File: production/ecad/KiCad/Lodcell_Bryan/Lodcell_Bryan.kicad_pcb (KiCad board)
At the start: 2 copper layers, 22 parts, among them J1 LoadCellConnector, J2 power_for_Loadcell, J3 ConnToESP32, U1 MIC920YC5-TR, U2 MIC920YC5-TR, U3 ADS1231IDR, U4 TXB0104DR

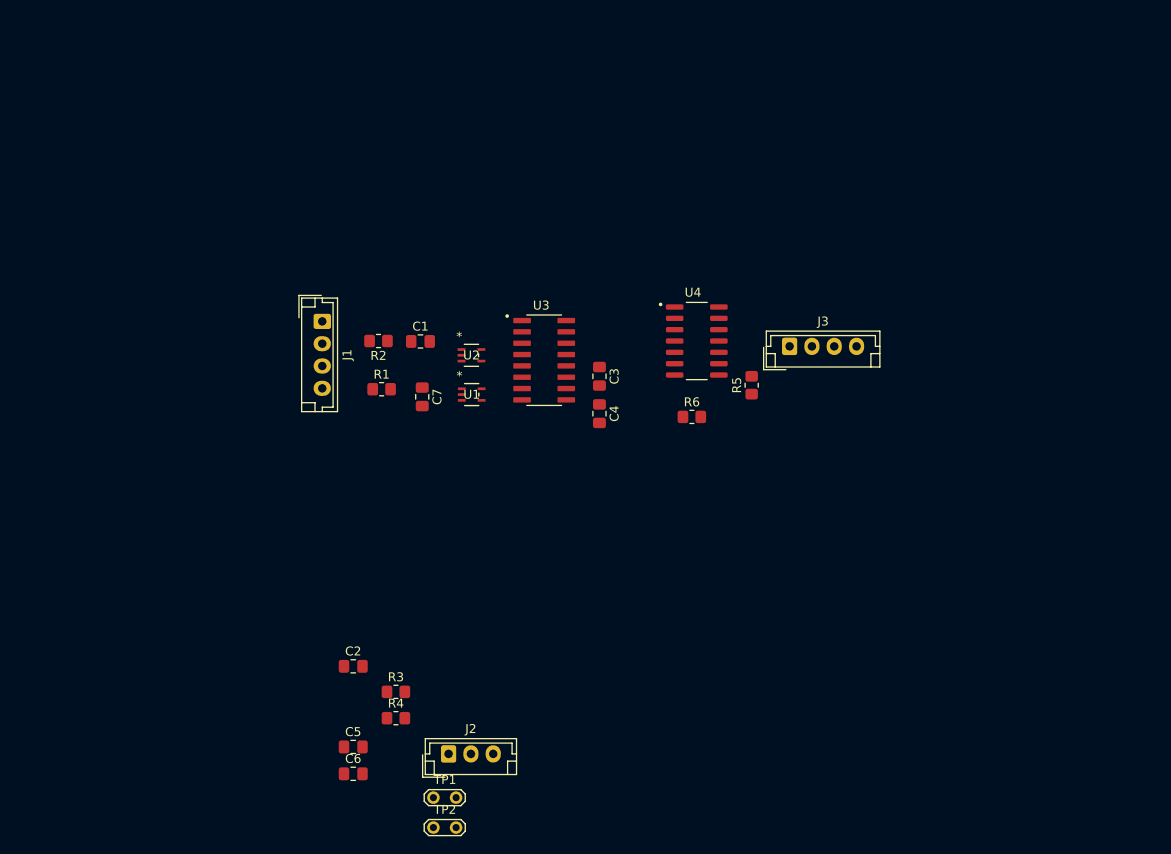
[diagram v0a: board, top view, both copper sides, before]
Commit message: Added mounting holes and very rough layout
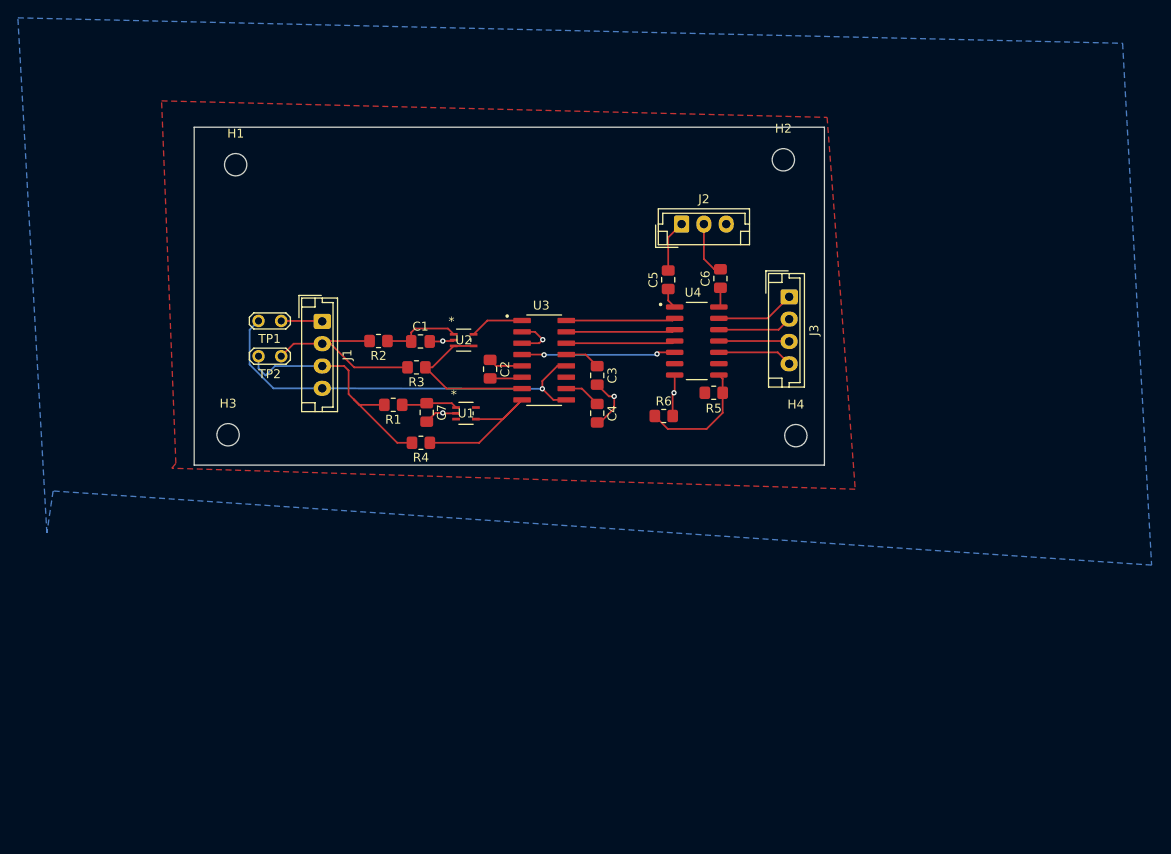
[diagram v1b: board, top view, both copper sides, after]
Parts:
- added H1: MountingHole, MountingHole:MountingHole_2.5mm, F.Cu at (129.8, 45.0)
- added H2: MountingHole, MountingHole:MountingHole_2.5mm, F.Cu at (191.2, 44.5)
- added H3: MountingHole, MountingHole:MountingHole_2.5mm, F.Cu at (129.0, 75.2)
- added H4: MountingHole, MountingHole:MountingHole_2.5mm, F.Cu at (192.6, 75.3)
- moved C6 69.1 mm to (184.2, 57.8), turned to 90 degrees
- moved J2 64.8 mm to (179.8, 51.6)
- moved C5 63.1 mm to (178.3, 57.9), turned to 90 degrees
- moved TP1 56.1 mm to (134.9, 62.5), turned to 180 degrees
- moved TP2 55.5 mm to (134.9, 66.5), turned to 180 degrees
- moved C2 36.7 mm to (158.3, 67.9), turned to -90 degrees
- moved R3 36.4 mm to (150.1, 67.7), turned to 180 degrees
- moved R4 31.0 mm to (150.6, 76.2), turned to 180 degrees
- moved J3 5.55 mm to (191.8, 59.8), turned to -90 degrees
- moved R5 4.33 mm to (183.4, 70.5), turned to 0 degrees
- moved R6 3.15 mm to (177.8, 73.2)
- moved U1 2.19 mm to (155.7, 72.8)
- moved R1 2.18 mm to (147.5, 71.9), turned to 180 degrees
- moved U2 1.91 mm to (155.4, 64.7)
- moved C7 1.82 mm to (151.2, 72.8)
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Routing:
- net Net-(J1-Pin_4): track 0.00 -> 46.7 mm, vias 0 -> 1
- net /RawLoadCell_-: track 0.00 -> 28.1 mm
- net +5V: track 0.00 -> 25.1 mm
- net GND: track 0.00 -> 22.7 mm, vias 0 -> 5
- net /RawLoadCell_+: track 0.00 -> 21.3 mm
- net /LP_-: track 0.00 -> 18.4 mm
- net /LP_+: track 0.00 -> 18.2 mm
- net Net-(U3-SPEED): track 0.00 -> 17.4 mm, vias 0 -> 2
- net Net-(U4-OE): track 0.00 -> 13.4 mm
- net Net-(U3-~{PDWN}): track 0.00 -> 12.2 mm
- net Net-(U3-SCLK): track 0.00 -> 12.2 mm
- net Net-(U3-~{DRDY}/DOUT): track 0.00 -> 12.2 mm
- net Net-(U2-IN+): track 0.00 -> 8.91 mm
- net MISO: track 0.00 -> 8.87 mm
- net Net-(J3-Pin_4): track 0.00 -> 8.41 mm
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- added copper zone on F.Cu, net +5V
- added copper zone on B.Cu, net GND
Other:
- board outline added: 70.6 x 37.9 mm

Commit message: Changes
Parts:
- C5, C6, R5, R6, U4: moved to B.Cu
- moved H3 59.5 mm to (185.0, 55.2)
- moved H1 49.5 mm to (179.3, 45.7)
- moved J3 38.2 mm to (158.5, 78.3), turned to 0 degrees
- moved C6 23.4 mm to (160.8, 60.3)
- moved R5 22.7 mm to (160.7, 70.2), turned to 90 degrees
- moved J2 20.0 mm to (160.7, 57.6)
- moved H4 19.7 mm to (192.2, 55.6)
- moved TP1 18.9 mm to (153.2, 57.4)
- moved TP2 18.8 mm to (152.1, 74.1)
- moved U4 15.9 mm to (165.6, 65.1), turned to 180 degrees
- moved R6 14.6 mm to (163.2, 71.5), turned to -90 degrees
- moved J1 11.1 mm to (150.7, 62.2)
- moved C5 11.0 mm to (167.4, 59.4), turned to 180 degrees
- moved R2 9.82 mm to (155.5, 63.0)
- moved C1 9.19 mm to (159.6, 63.0)
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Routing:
- net Net-(J1-Pin_4): track 46.7 -> 0.00 mm, vias 1 -> 0
- net /RawLoadCell_-: track 28.1 -> 0.00 mm
- net GND: track 22.7 -> 0.00 mm, vias 5 -> 0
- net /RawLoadCell_+: track 21.3 -> 0.00 mm
- net /LP_-: track 18.4 -> 0.00 mm
- net /LP_+: track 18.2 -> 0.00 mm
- net Net-(U3-SPEED): track 17.4 -> 0.00 mm, vias 2 -> 1
- net +5V: track 25.1 -> 7.89 mm
- net Net-(U4-OE): track 13.4 -> 0.00 mm
- net Net-(U3-~{DRDY}/DOUT): track 12.2 -> 2.66 mm
- net Net-(U3-SCLK): track 12.2 -> 2.75 mm
- net Net-(U3-~{PDWN}): track 12.2 -> 2.82 mm
- net Net-(U2-IN+): track 8.91 -> 0.00 mm
- net MISO: track 8.87 -> 0.00 mm
- net Net-(J3-Pin_4): track 8.41 -> 0.00 mm
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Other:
- board size 70.6 x 37.9 mm -> 33.3 x 33.3 mm
- board text added: "+3.3"
- board text added: "+5"
- board text added: "-"
- board text added: "LoadCell"

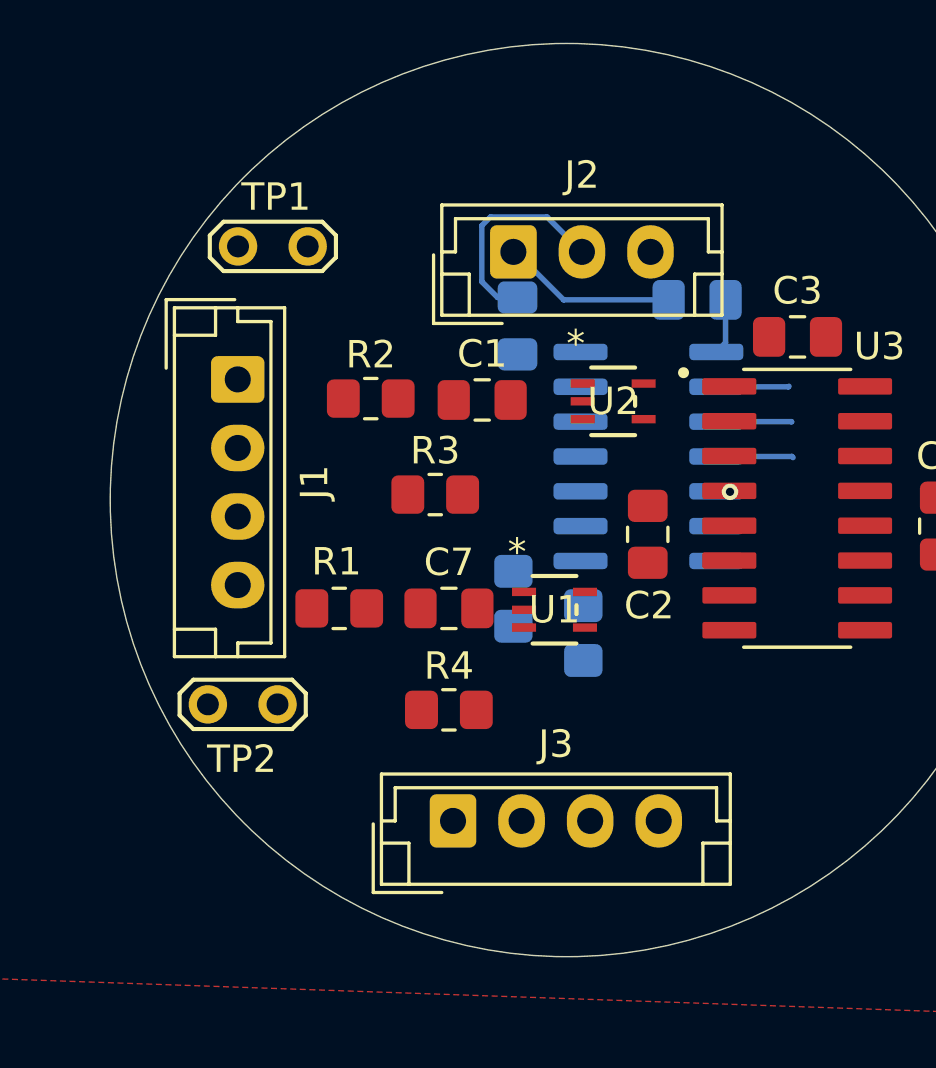
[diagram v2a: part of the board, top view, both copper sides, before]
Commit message: load cell footprint updates
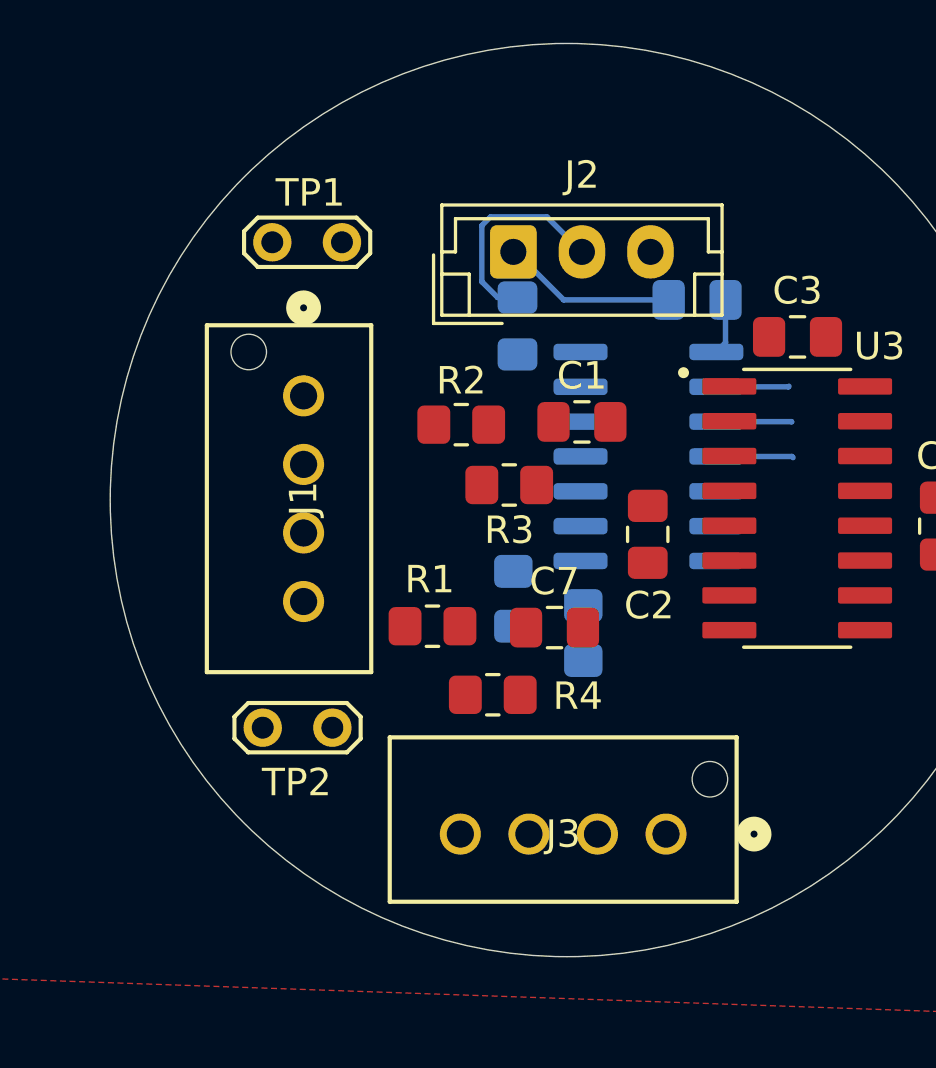
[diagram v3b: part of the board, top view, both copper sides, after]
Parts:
- removed U1, U2: MIC920YC5-TR, MIC920YC5-TR:SC-70_C5_MCH
- H1: value MountingHole -> UpperLeftMH
- H2: value MountingHole -> UpperRightMH
- H3: value MountingHole -> BottomLeftMH
- H4: value MountingHole -> LowerRightMH
- J1, J3: footprint Connector_JST:JST_EH_B4B-EH-A_1x04_P2.50mm_Vertical -> CONN_B4B-XH-AM_JST:CONN_B4B-XH-AM_JST
- moved J3 7.78 mm to (166.3, 78.8)
- moved C7 3.91 mm to (162.2, 71.3)
- moved C1 3.72 mm to (163.2, 63.8)
- moved R1 3.46 mm to (157.8, 71.2)
- moved R2 3.43 mm to (158.8, 63.9)
- moved R3 2.72 mm to (160.6, 66.1)
- moved J1 2.47 mm to (153.1, 62.9), turned to 90 degrees
- moved TP2 2.17 mm to (154.1, 75.0)
- moved R4 1.69 mm to (159.9, 73.8)
- moved TP1 1.26 mm to (154.4, 57.2)
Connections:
- net Net-(J3-Pin_4) renamed SPEED
- C1 pad 1: Net-(U2-IN+) -> /LP_+
- C7 pad 1: Net-(U1-IN+) -> GND
- C7 pad 2: GND -> /LP_-
- R1 pad 1: Net-(U1-IN+) -> /LP_-
- R2 pad 1: Net-(U2-IN+) -> /LP_+
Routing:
- net Net-(U3-SPEED): vias 1 -> 0

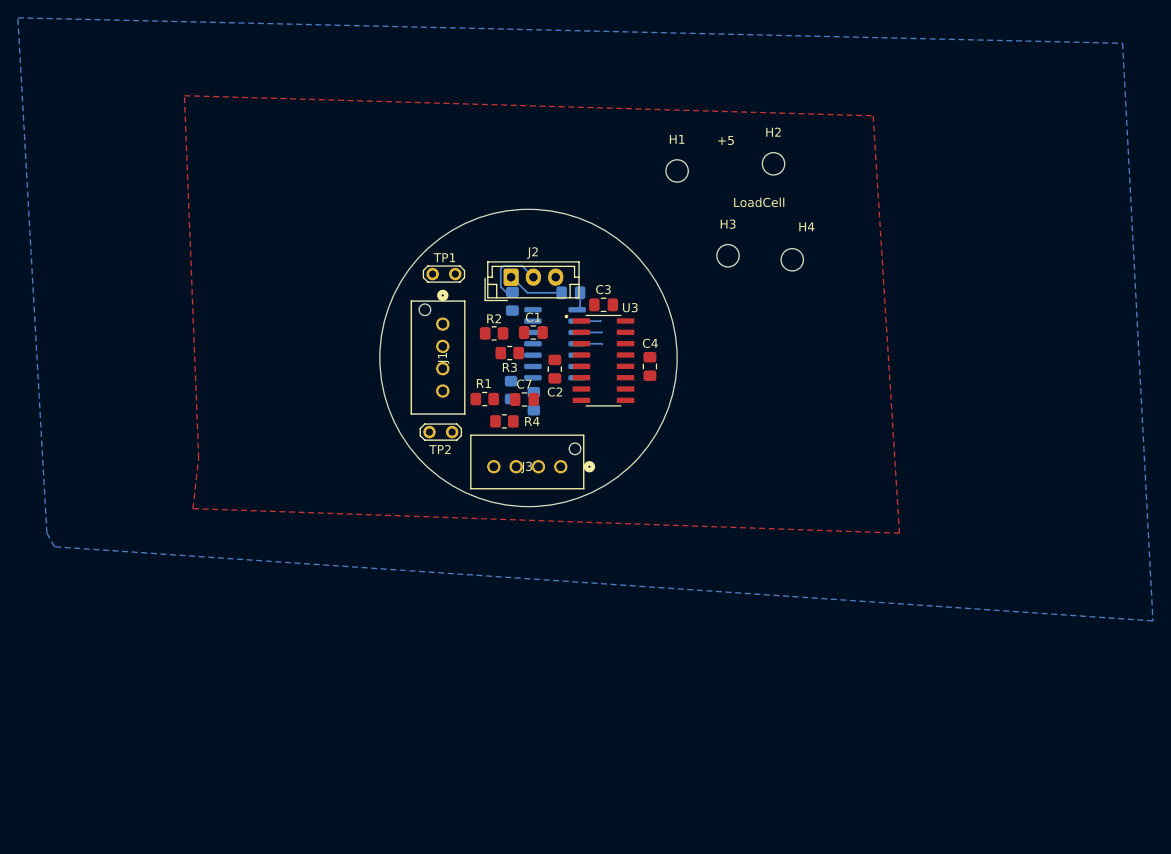
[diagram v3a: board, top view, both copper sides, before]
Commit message: Layout for loadcell
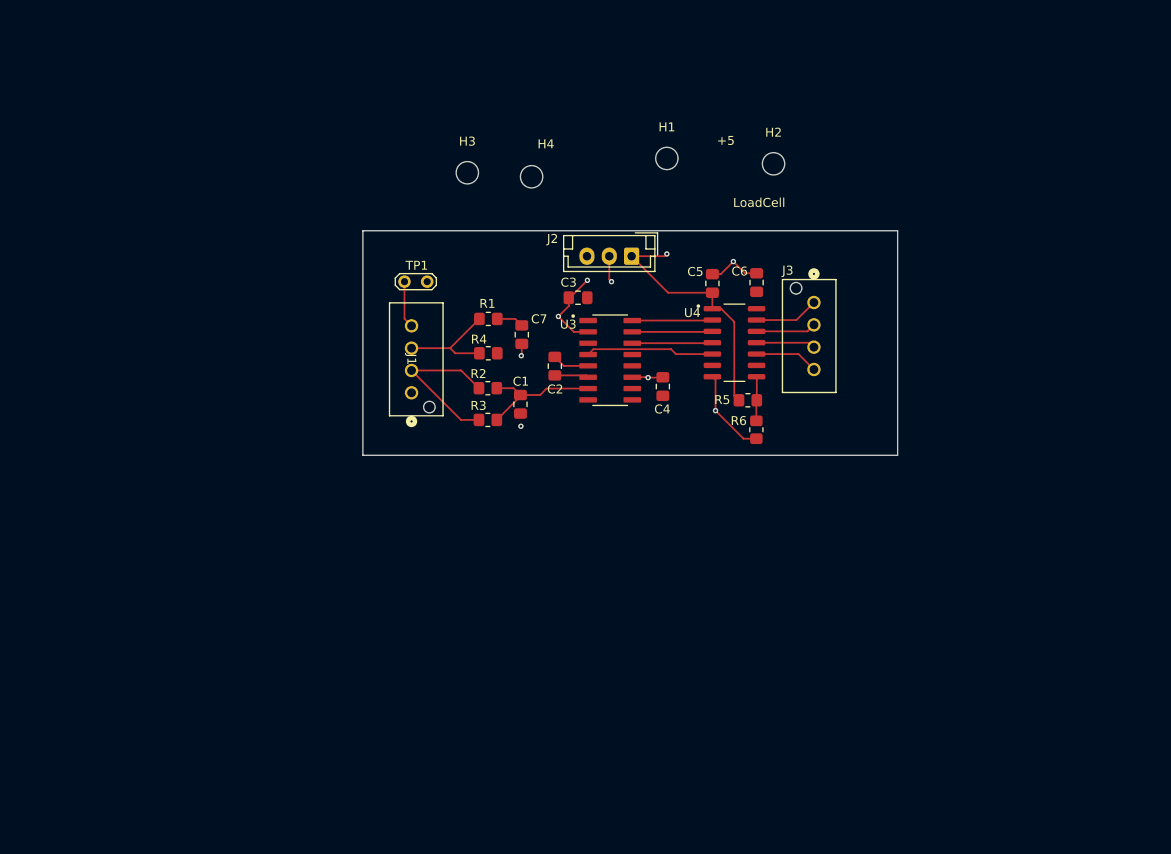
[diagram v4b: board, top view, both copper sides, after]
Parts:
- removed TP2: TestPoint_LoadCellSignal, TestPoint:TestPoint_2Pads_Pitch2.54mm_Drill0.8mm
- C5, C6, R5, R6, U4: moved to F.Cu
- moved J3 33.8 mm to (194.6, 60.4), turned to 90 degrees
- moved H3 30.6 mm to (155.8, 45.9)
- moved H4 30.6 mm to (163.0, 46.4)
- moved C6 27.4 mm to (188.2, 58.2), turned to -90 degrees
- moved R5 26.5 mm to (187.2, 71.4), turned to 0 degrees
- moved R6 25.1 mm to (188.2, 74.7)
- moved U4 20.1 mm to (185.7, 64.9), turned to 0 degrees
- moved C5 15.9 mm to (183.2, 58.3), turned to -90 degrees
- moved J2 13.7 mm to (174.2, 55.2), turned to 180 degrees
- moved R1 8.98 mm to (158.2, 62.3)
- moved J1 8.46 mm to (149.6, 70.5), turned to -90 degrees
- moved C1 8.17 mm to (161.8, 71.8), turned to -90 degrees
- moved R3 7.88 mm to (158.1, 73.6)
- moved R4 7.83 mm to (158.2, 66.1)
- moved C7 7.27 mm to (161.9, 64.0), turned to 90 degrees
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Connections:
- C5 pad 1: Net-(U4-VCCA) -> GND
- C6 pad 1: Net-(U4-VCCB) -> GND
- U4 pad 1: Net-(U4-VCCA) -> +3.3V
- U4 pad 14: Net-(U4-VCCB) -> +5V
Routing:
- net GND: track 0.00 -> 33.0 mm, vias 0 -> 7
- net +3.3V: track 6.39 -> 28.7 mm, vias 0 -> 1
- net /RawLoadCell_+: track 0.00 -> 18.2 mm
- net /LP_+: track 0.00 -> 14.7 mm
- net Net-(U3-SPEED): track 0.00 -> 14.4 mm
- net /RawLoadCell_-: track 0.00 -> 12.5 mm
- net MISO: track 0.00 -> 7.24 mm
- net SPEED: track 0.00 -> 7.14 mm
- net CLK: track 0.00 -> 6.73 mm
- net PDWN: track 0.00 -> 6.63 mm
- net Net-(U3-~{DRDY}/DOUT): track 2.66 -> 9.00 mm
- net Net-(U3-SCLK): track 2.75 -> 9.00 mm
- net Net-(U3-~{PDWN}): track 2.82 -> 9.00 mm
- net Net-(J1-Pin_4): track 0.00 -> 5.28 mm
- net Net-(U4-OE): track 0.00 -> 4.97 mm
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- added copper zone on In1.Cu, net +3.3V
- added copper zone on In1.Cu, net +5V
- added copper zone on In2.Cu, net GND
- removed copper zone on F.Cu, net +5V
- removed copper zone on B.Cu, net GND
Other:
- board size 33.3 x 33.3 mm -> 59.9 x 25.1 mm
- copper layers 2 -> 4

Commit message: More layout changes
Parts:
- moved TP1 1.00 mm to (151.3, 57.1)
- moved C1 0.90 mm to (161.4, 71.0)
- moved C7 0.85 mm to (161.9, 63.2)
- moved R4 0.28 mm to (158.2, 65.8)
- moved J2 0.14 mm to (174.1, 55.1)
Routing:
- net +5V: track 2.95 -> 61.1 mm
- net +3.3V: track 28.7 -> 5.91 mm, vias 1 -> 2
- net /LP_-: track 3.05 -> 19.3 mm, vias 0 -> 2
- net /LP_+: track 14.7 -> 20.6 mm
- net Net-(J1-Pin_4): track 5.28 -> 9.65 mm, vias 0 -> 2
- net GND: track 33.0 -> 28.9 mm, vias 7 -> 6
- added copper zone on B.Cu, net /LP_-
- added copper zone on F.Cu, net Net-(J1-Pin_4)
- added copper zone on In2.Cu, net Net-(J1-Pin_4)
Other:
- board size 59.9 x 25.1 mm -> 56.2 x 25.1 mm
- board text removed: "+3.3"
- board text removed: "+5"
- board text removed: "-"
- board text removed: "LoadCell"

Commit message: Improved load cell layout
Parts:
- moved J1 10.1 mm to (151.1, 60.6), turned to 90 degrees
- moved R3 9.14 mm to (158.0, 64.4)
- moved R2 9.14 mm to (158.0, 60.9)
- moved C1 9.14 mm to (161.4, 61.8)
- moved R4 6.23 mm to (157.9, 72.1)
- moved R1 6.23 mm to (157.9, 68.5)
- moved C7 6.23 mm to (161.7, 69.4)
- moved TP1 1.70 mm to (151.3, 55.4)
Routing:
- net /RawLoadCell_+: track 18.2 -> 0.16 mm
- net /LP_+: track 20.6 -> 3.18 mm
- net /LP_-: track 19.3 -> 7.70 mm, vias 2 -> 1
- net /RawLoadCell_-: track 12.4 -> 15.6 mm
- net GND: track 28.9 -> 27.5 mm, vias 6 -> 5
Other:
- board size 56.2 x 25.1 mm -> 50.7 x 25.1 mm
